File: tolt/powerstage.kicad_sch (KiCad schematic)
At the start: 131 parts, among them Q1 NMOS, Q10 NMOS, Q11 NMOS, Q12 NMOS, Q13 NMOS, Q14 NMOS, Q15 NMOS, Q16 NMOS, Q17 NMOS, Q18 NMOS, Q2 NMOS, Q3 NMOS, Q4 NMOS, Q5 NMOS, Q6 NMOS, Q7 NMOS, Q8 NMOS, Q9 NMOS

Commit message: sch cleanup
cleaned fet sheet and added ferrite bead
Fixed some ground issues
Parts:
- added FB1, FB10, FB11, FB12, FB13, FB14, FB15, FB16, FB17, FB18, FB2, FB3, FB4, FB5, FB6, FB7, FB8, FB9: FerriteBead, symbol Device:FerriteBead
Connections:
- net Ph_a: now also R105.1; no longer R105.2
- net Ph_b: now also R108.1; no longer R108.2
- net Ph_c: now also R111.1; no longer R111.2
- net at D20.2 (A), Q17.2 (G), R92.2: now also FB4.2; no longer R28.2
- net at D11.2 (A), Q8.2 (G), R107.1: now also FB9.2; no longer R15.2
- net at D8.2 (A), Q2.2 (G), R104.1: now also FB14.2; no longer R6.2
- net at D9.2 (A), Q1.2 (G), R103.2: now also FB13.2; no longer R7.1
- net at D15.2 (A), Q10.2 (G), R88.2: now also FB8.2; no longer R19.1
- net at D6.2 (A), Q4.2 (G), R85.2: now also FB16.2; no longer R10.1
- net at D16.2 (A), Q15.2 (G): now also R111.2, FB1.2; no longer R111.1, R23.2
- net at D14.2 (A), Q11.2 (G), R89.2: now also FB10.2; no longer R18.2
- net at D4.2 (A), Q6.2 (G), R87.2: now also FB18.2; no longer R8.2
- net at D7.2 (A), Q3.2 (G): now also R105.2, FB15.2; no longer R105.1, R5.2
- net at D21.2 (A), Q16.2 (G), R91.2: now also FB6.2; no longer R29.1
- net at D19.2 (A), Q18.2 (G), R93.2: now also FB2.2; no longer R27.2
- net at D13.2 (A), Q12.2 (G), R90.2: now also FB12.2; no longer R17.2
- net at D18.2 (A), Q13.2 (G), R109.2: now also FB5.2; no longer R25.1
- net at D10.2 (A), Q9.2 (G): now also R108.2, FB11.2; no longer R108.1, R14.2
- net at D17.2 (A), Q14.2 (G), R110.1: now also FB3.2; no longer R24.2
- net at D5.2 (A), Q5.2 (G), R86.2: now also FB17.2; no longer R9.2
- net at D12.2 (A), Q7.2 (G), R106.2: now also FB7.2; no longer R16.1
- new net: FB17.1, R9.2
- new net: FB3.1, R24.2
- new net: FB13.1, R7.1
- new net: FB14.1, R6.2
- new net: FB1.1, R23.2
- new net: FB7.1, R16.1
- new net: FB4.1, R28.2
- new net: FB10.1, R18.2
- new net: FB8.1, R19.1
- new net: FB6.1, R29.1
- new net: FB16.1, R10.1
- new net: FB12.1, R17.2
- new net: FB5.1, R25.1
- new net: FB18.1, R8.2
- new net: FB11.1, R14.2
- new net: FB9.1, R15.2
- new net: FB2.1, R27.2
- new net: FB15.1, R5.2
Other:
- moved on the sheet: C100, C101, C102, C103, C104, C105, C106, C107, C108, C109, C110, C111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

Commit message: finished routing
AAAAAAAAAAAAAAAAaaAAAAAAAAAAAAAAAAaaAAAAAAAAAAAAAAAAaaAAAAAAAAAAAAAAAAaaAAAAAAAAAAAAAAAAaaAAAAAAAAAAAAAAAAaaAAAAAAAAAAAAAAAAaaAAAAAAAAAAAAAAAAaaAAAAAAAAAAAAAAAAaaAAAAAAAAAAAAAAAAaaAAAAAAAAAAAAAAAAaa

PLZ WORK PLZ WORK PLZ WORK PLZ WORK PLZ WORK PLZ WORK PLZ WORK PLZ WORK PLZ WORK PLZ WORK PLZ WORK PLZ WORK PLZ WORK PLZ WORK PLZ WORK PLZ WORK PLZ WORK PLZ WORK PLZ WORK PLZ WORK PLZ WORK PLZ WORK PLZ WORK PLZ WORK PLZ WORK PLZ WORK PLZ WORK PLZ WORK PLZ WORK PLZ WORK PLZ WORK PLZ WORK PLZ WORK PLZ WORK PLZ WORK
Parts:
- removed C102, C105, C111: 1uf, Capacitor_SMD:C_2220_5750Metric_Pad1.97x5.40mm_HandSolder, symbol Device:C
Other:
- note added: "Ferrite beads value needs to be calculated according to measurements. Note : most likely the value will be different on top and bottom gate"

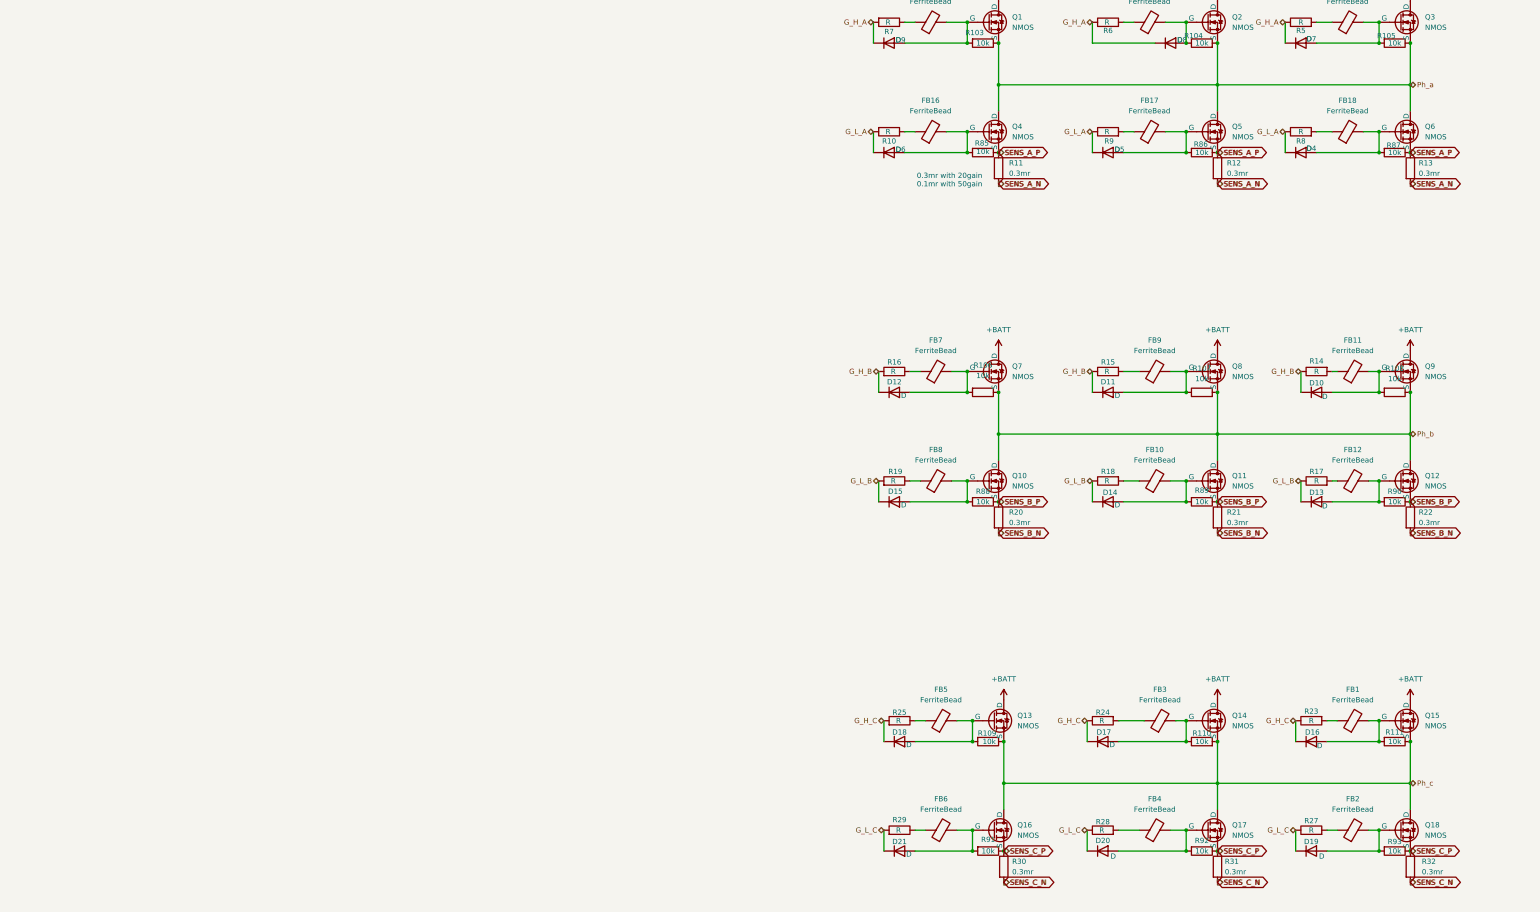
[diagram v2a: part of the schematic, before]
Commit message: big update
fixed decoupling correctly
more gnd plane work and routing finished
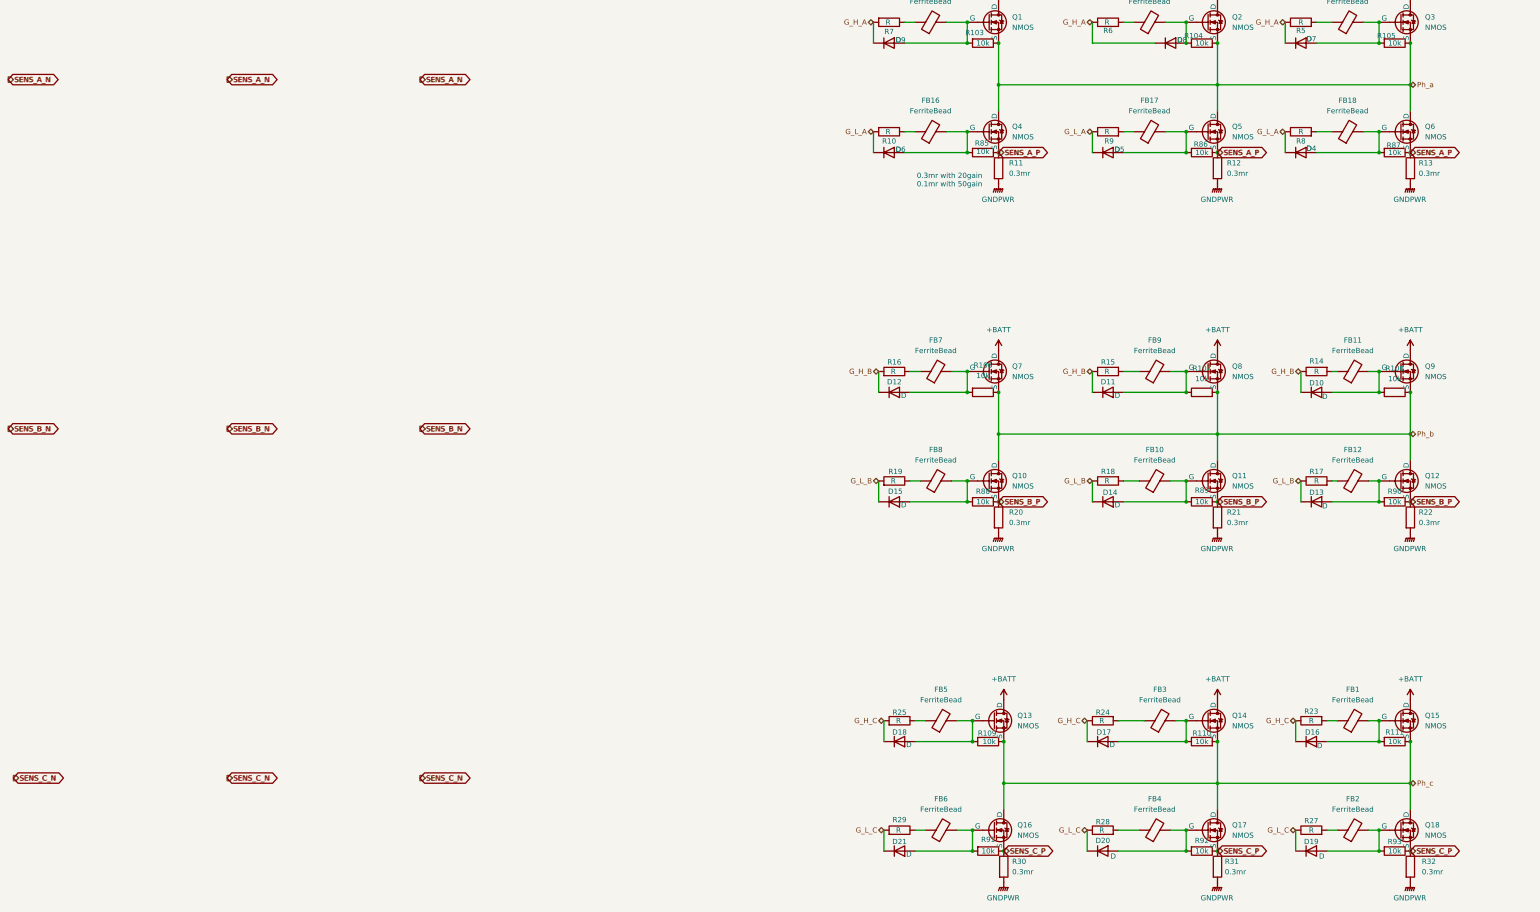
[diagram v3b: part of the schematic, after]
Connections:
- net GNDPWR: now also R11.2, R12.2, R13.2, R20.2, R21.2, R22.2, R30.2, R31.2, R32.2
- net SENS_A_N: no longer R11.2, R12.2, R13.2
- net SENS_B_N: no longer R20.2, R21.2, R22.2
- net SENS_C_N: no longer R30.2, R31.2, R32.2

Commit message: begenning of lcsc part assign
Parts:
- C101, C103, C104, C106, C107, C108, C109, C110, C112, C113, C114, C115, C128, C129, C130, C131, C132, C133, C134, C135, C136, C137, C138, C139, C140, C141, C142: footprint Capacitor_SMD:C_2220_5750Metric_Pad1.97x5.40mm_HandSolder -> Capacitor_SMD:C_2220_5750Metric
- D10, D11, D12, D13, D14, D15, D16, D17, D18, D19, D20, D21, D4, D5, D6, D7, D8, D9: LCSC (none) -> C83528
- FB1, FB10, FB11, FB12, FB13, FB14, FB15, FB16, FB17, FB18, FB2, FB3, FB4, FB5, FB6, FB7, FB8, FB9: footprint (none) -> Capacitor_SMD:C_0603_1608Metric
- R103, R104, R105, R106, R107, R108, R109, R110, R111, R61, R62, R63, R85, R86, R87, R88, R89, R90, R91, R92, R93: LCSC (none) -> C25804

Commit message: more assign+12-5v change
changed with TPS82130
Since using esp32 will increase consumption by a lot
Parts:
- R58, R59, R60: LCSC (none) -> C13564
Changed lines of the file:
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@@
 			)
 		)
+		(property "LCSC" "C13564"
+			(at 381 220.98 0)
+			(effects
+				(font
+					(size 1.27 1.27)
+				)
+				(hide yes)
+			)
+		)
 		(pin "1"
 		)
@@
 			)
 		)
+		(property "LCSC" "C13564"
+			(at 347.98 220.98 0)
+			(effects
+				(font
+					(size 1.27 1.27)
+				)
+				(hide yes)
+			)
+		)
 		(pin "1"
 		)
@@
 			(at 317.5 220.98 0)
 			(effects
+				(font
+					(size 1.27 1.27)
+				)
+				(hide yes)
+			)
+		)
+		(property "LCSC" "C13564"
+			(at 317.5 220.98 0)
+			(effects

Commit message: hm
weird huh it didnt fucking save
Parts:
- C101, C103, C104, C106, C107, C108, C109, C110, C112, C113, C114, C115, C128, C129, C130, C131, C132, C133, C134, C135, C136, C137, C138, C139, C140, C141, C142: LCSC (none) -> C153032
- C58, C59, C60: LCSC (none) -> C913904
- R11, R12, R13, R20, R21, R22, R30, R31, R32: LCSC (none) -> C49325908

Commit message: fab
finally.
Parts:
- FB1, FB10, FB11, FB12, FB13, FB14, FB15, FB16, FB17, FB18, FB2, FB3, FB4, FB5, FB6, FB7, FB8, FB9: LCSC (none) -> C17305
- R10, R14, R15, R16, R17, R18, R19, R23, R24, R25, R27, R28, R29, R5, R6, R7, R8, R9: value R -> 24r; LCSC (none) -> C5560548
